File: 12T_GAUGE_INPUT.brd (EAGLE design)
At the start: 69.1 x 60 mm, 99 parts, among them J1 MICRO-SD_CARD_SOCKET, P1_WP_PULLUP 10k, P2_WP_PULLUP 10k, P3_WP_PULLUP 10k

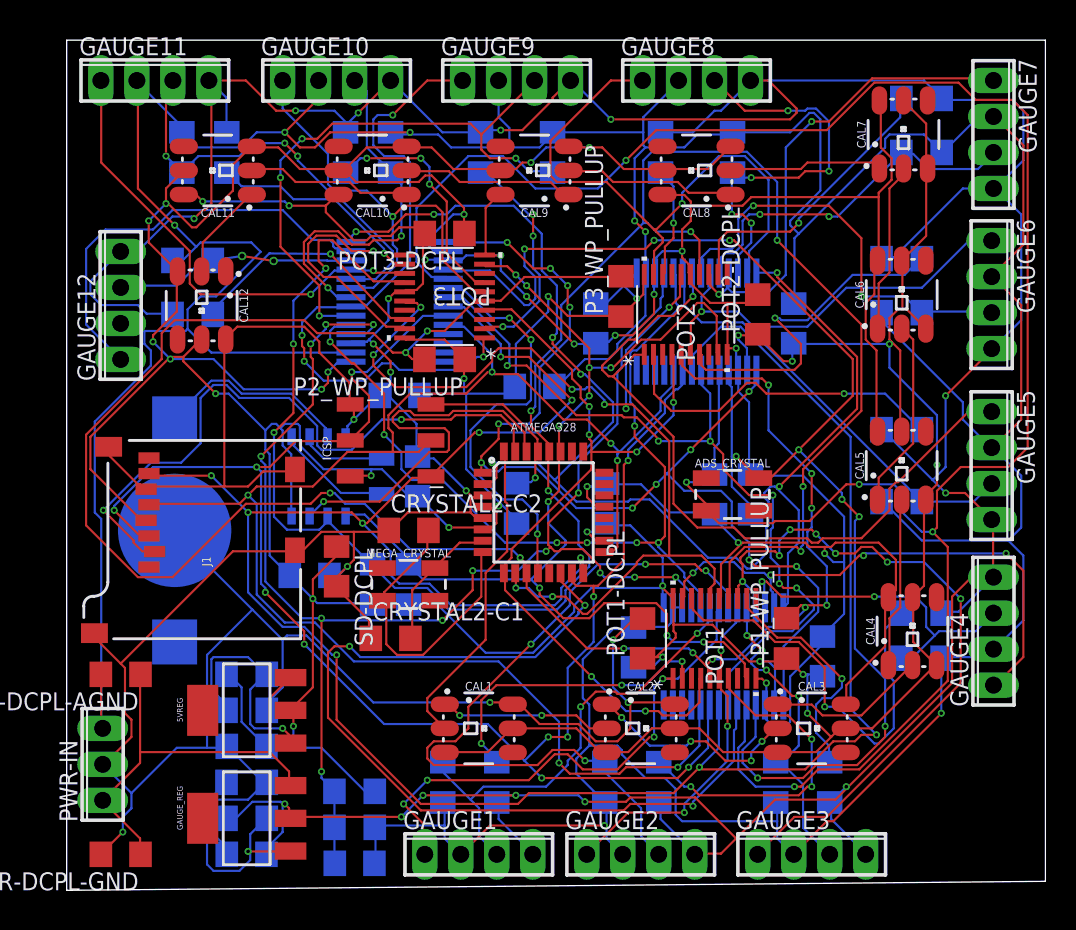
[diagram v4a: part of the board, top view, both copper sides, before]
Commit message: Converted to 4 layer board
Down to 2.3x2.7
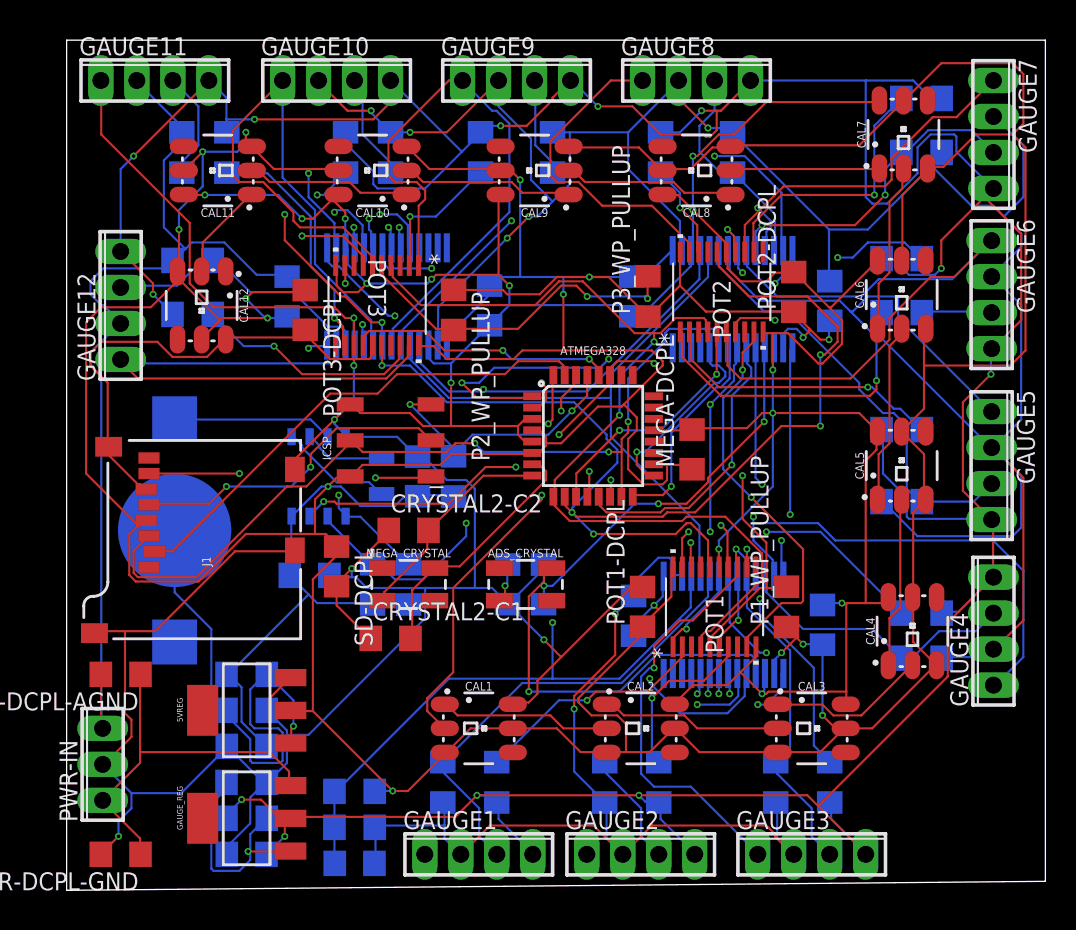
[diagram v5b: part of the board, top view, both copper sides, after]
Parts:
- moved ADS3-DCPL1 18.6 mm to (15.6, 41.9), turned to 90 degrees
- moved ADS_CRYSTAL 15.9 mm to (32.4, 21.6)
- moved CRYSTAL1-C1 15.9 mm to (31.1, 21.6)
- moved CRYSTAL1-C2 15.9 mm to (33.7, 21.6)
- moved POT3-DCPL 11.2 mm to (16.8, 41.0), turned to 270 degrees
- moved ADS3-DCPL2 8.98 mm to (29.8, 41.3), turned to 270 degrees
- moved MEGA-DCPL 7.13 mm to (44.1, 31.1), flipped to the top
- moved ATMEGA328 6.43 mm to (37.1, 32.1)
- moved MEGA_RESET_PULLUP 4.84 mm to (27.3, 29.2)
- moved POT3 4.80 mm to (21.9, 41.3), turned to 270 degrees
- moved P2_WP_PULLUP 3.55 mm to (27.3, 41.0), turned to 270 degrees
- moved ADS2-DCPL2 3.17 mm to (39.9, 41.9)
- moved ADS2 3.00 mm to (47.0, 41.7)
- moved ADS2-DCPL1 3.00 mm to (53.8, 41.6)
- moved POT2 3.00 mm to (46.2, 42.2)
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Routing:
- net MISO: track 173.3 -> 97.8 mm, vias 10 -> 5
- net WP: track 145.3 -> 73.2 mm, vias 12 -> 5
- net SCL: track 146.1 -> 81.8 mm, vias 9 -> 5
- net XTAL1: track 156.5 -> 95.2 mm, vias 5 -> 4
- net +5V: track 428.6 -> 488.4 mm, vias 28 -> 17
- net ADS1_CS: track 64.9 -> 24.3 mm, vias 3 -> 2
- net ADS_SYNC: track 99.0 -> 75.9 mm, vias 7 -> 4
- net ADS2_CS: track 0.00 -> 20.6 mm, vias 0 -> 1
- net B2+: track 52.3 -> 32.3 mm, vias 4 -> 1
- net MOSI: track 122.2 -> 102.4 mm, vias 11 -> 5
- net B6-_P2W1: track 29.8 -> 47.3 mm, vias 1 -> 0
- net B3-_P1W2: track 50.3 -> 32.8 mm, vias 7 -> 2
- net AINCOM: track 61.6 -> 44.8 mm, vias 7 -> 0
- net VREF: track 103.0 -> 87.6 mm, vias 13 -> 2
- net XTAL2: track 102.2 -> 87.3 mm, vias 9 -> 5
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
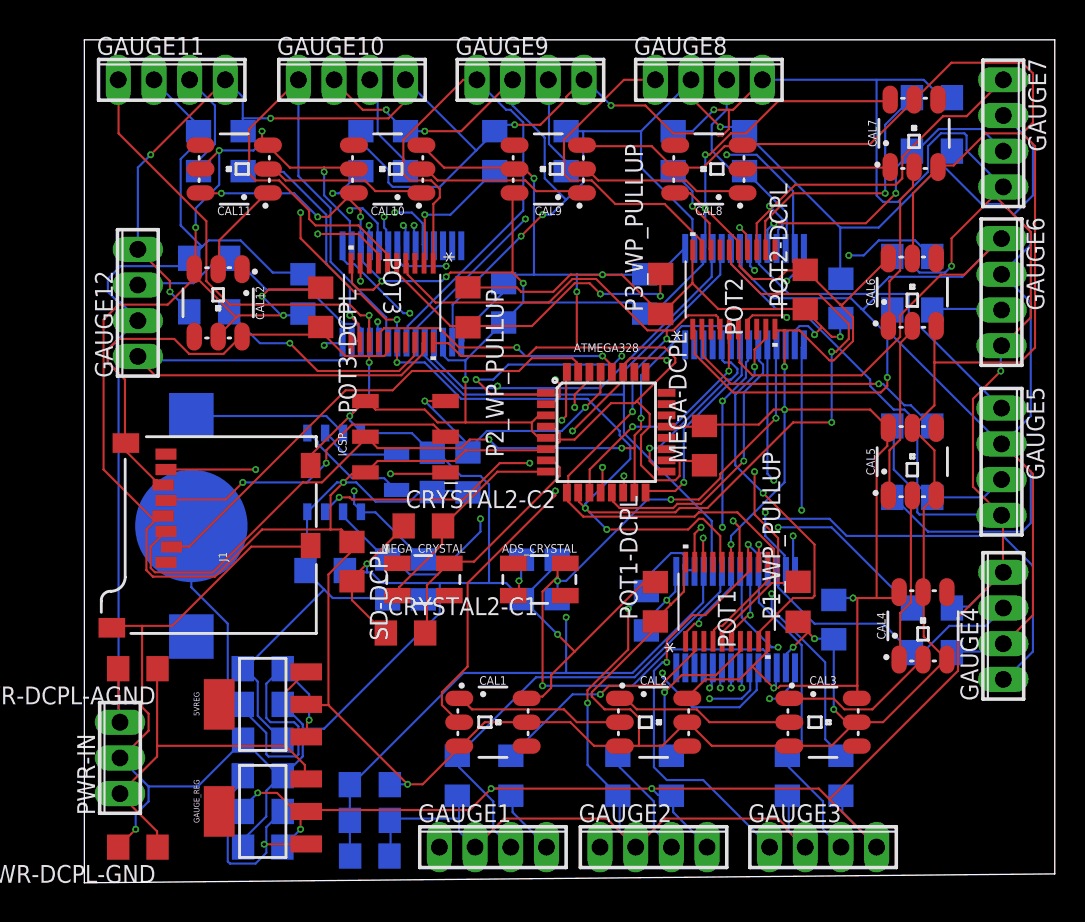
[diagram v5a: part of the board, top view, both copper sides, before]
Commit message: 4 Layer Size Optimization 2
Now 2.4x2.3
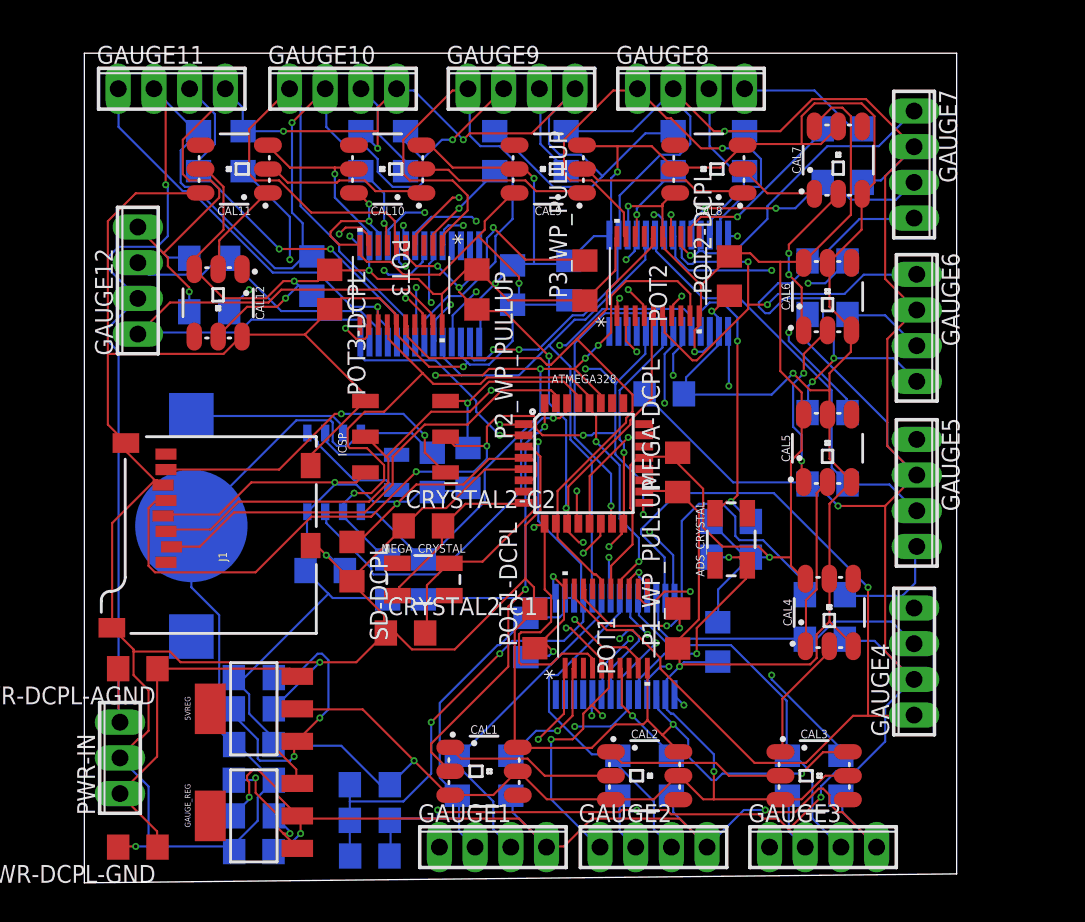
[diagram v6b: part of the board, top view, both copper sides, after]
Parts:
- moved CRYSTAL1-C1 15.0 mm to (46.0, 23.2), turned to 180 degrees
- moved ADS2-DCPL1 14.3 mm to (41.3, 34.8), turned to 0 degrees
- moved ADS_CRYSTAL 13.9 mm to (46.0, 24.4), turned to 90 degrees
- moved CRYSTAL1-C2 13.1 mm to (46.0, 25.7), turned to 0 degrees
- moved ADS1-DCPL1 8.78 mm to (31.4, 17.5)
- moved ADS1 8.78 mm to (37.8, 16.8)
- moved P1_WP_PULLUP 8.78 mm to (42.2, 18.1)
- moved POT1 8.78 mm to (37.1, 18.1)
- moved POT1-DCPL 8.78 mm to (32.1, 18.1)
- moved ADS1-DCPL2 8.41 mm to (45.1, 17.1)
- moved B4-R1 7.68 mm to (52.7, 17.3)
- moved B4-R2 7.68 mm to (52.7, 20.5)
- moved GAUGE4 6.84 mm to (59.1, 15.7)
- moved CAL4 6.74 mm to (53.0, 19.2)
- moved B7-R1 6.73 mm to (54.0, 49.8)
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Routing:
- net +5V: track 488.4 -> 398.2 mm, vias 17 -> 16
- net POT_SELECT_1: track 80.0 -> 47.3 mm, vias 5 -> 0
- net XTAL1: track 95.2 -> 65.0 mm
- net B4-_P1W3: track 42.0 -> 66.3 mm, vias 2 -> 1
- net GND: track 421.3 -> 442.5 mm, vias 19 -> 12
- net ADS_SYNC: track 75.9 -> 56.2 mm, vias 4 -> 3
- net VREF: track 87.6 -> 72.2 mm, vias 2 -> 5
- net B6-_P2W1: track 47.3 -> 32.4 mm, vias 0 -> 2
- net B5-_P2W0: track 48.9 -> 35.6 mm, vias 1 -> 2
- net XTAL2: track 87.3 -> 74.9 mm, vias 5 -> 4
- net AGND: track 355.3 -> 366.5 mm, vias 7 -> 10
- net MOSI: track 102.4 -> 91.6 mm, vias 5 -> 4
- net MISO: track 97.8 -> 87.2 mm, vias 5 -> 6
- net B1+: track 33.2 -> 23.6 mm
- net P1B3: track 19.3 -> 28.8 mm, vias 2 -> 1
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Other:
- board size 69.1 x 60 mm -> 62.1 x 59 mm

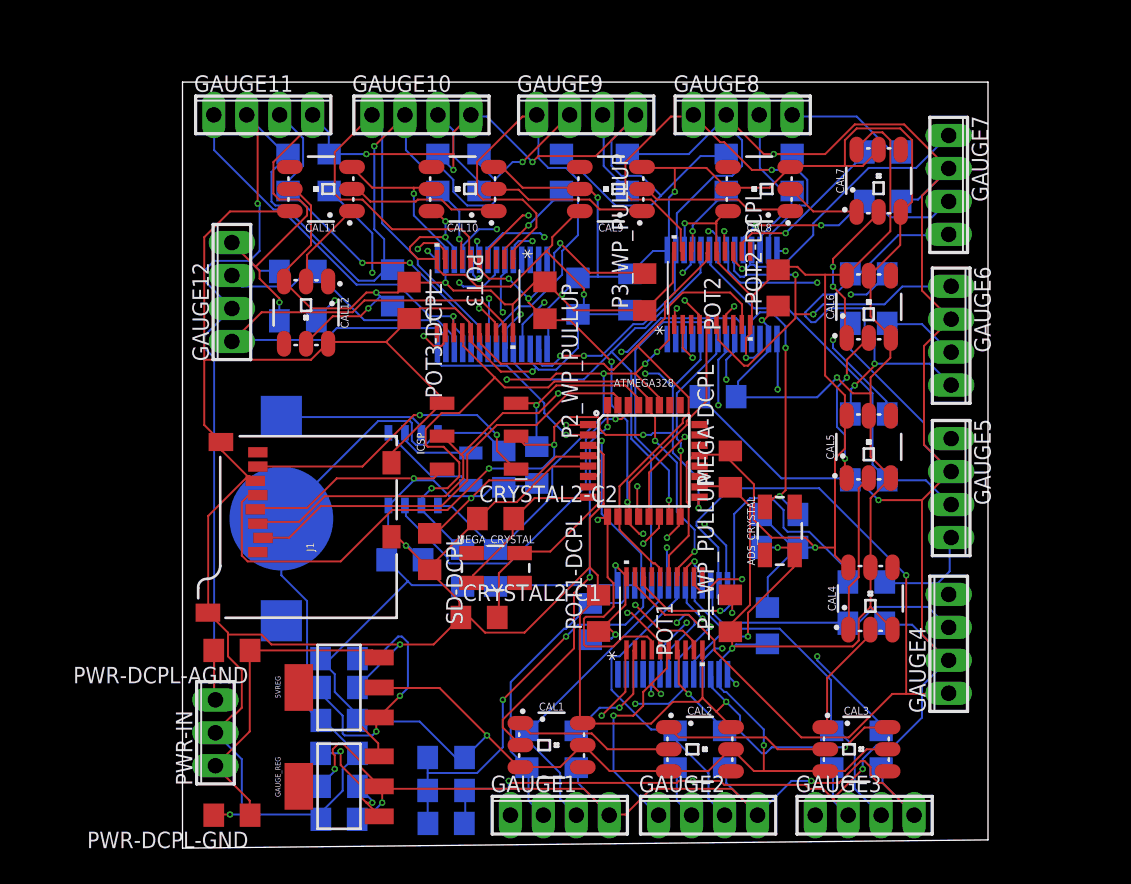
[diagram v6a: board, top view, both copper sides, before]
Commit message: Added in R3 to bridges
2.4x2.8"
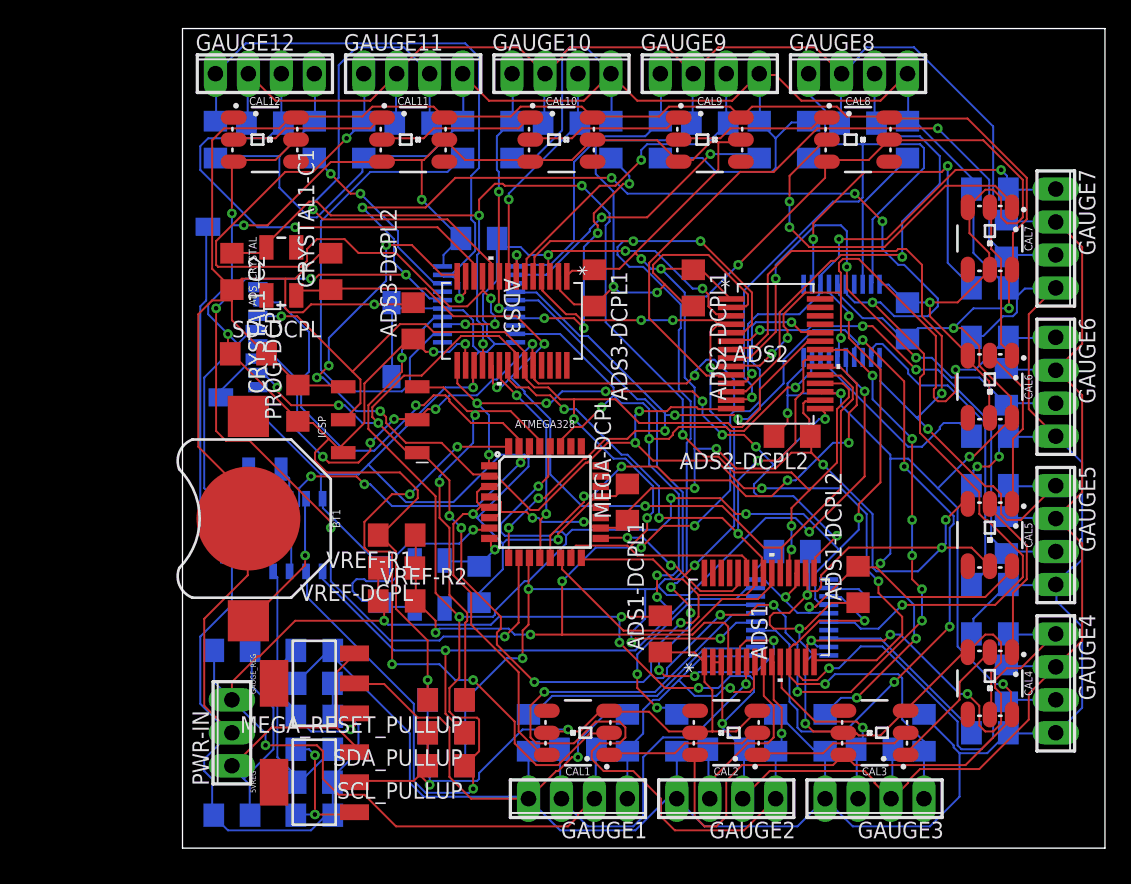
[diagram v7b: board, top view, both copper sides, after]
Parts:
- added B10R3, B11R3, B12R3, B1R3, B2R3, B3R3, B4R3, B5R3, B6R3, B7R3, B8R3, B9R3: 370, rcl:R1206
- moved CRYSTAL1-C2 46.2 mm to (3.81, 44.5), flipped to the top, turned to 270 degrees
- moved ADS_CRYSTAL 43.3 mm to (7.62, 44.5)
- moved CRYSTAL1-C1 40.6 mm to (11.4, 44.5), flipped to the top, turned to 90 degrees
- moved P3_WP_PULLUP 35.0 mm to (20.3, 11.4), flipped to the bottom, turned to 180 degrees
- moved P2_WP_PULLUP 34.2 mm to (20.3, 8.89), flipped to the bottom, turned to 180 degrees
- moved P1_WP_PULLUP 24.9 mm to (20.3, 6.35), flipped to the bottom, turned to 180 degrees
- moved SD-DCPL 20.7 mm to (5.08, 38.1), turned to 0 degrees
- moved VREF-DCPL 20.1 mm to (16.5, 21.6), flipped to the top
- moved MEGA_RESET_PULLUP 19.4 mm to (20.3, 11.4), flipped to the top, turned to 180 degrees
- moved VREF-R1 17.6 mm to (16.5, 24.1), flipped to the top
- moved GAUGE12 17.0 mm to (6.35, 59.7), turned to 0 degrees
- moved ADS2-DCPL2 16.7 mm to (47.0, 31.8), flipped to the top, turned to 180 degrees
- moved PROG-DCPL 16.7 mm to (8.89, 34.3), flipped to the top
- moved B5-R2 16.1 mm to (62.2, 20.3), turned to 0 degrees
- moved RTC_CRYSTAL 15.9 mm to (6.35, 29.2), turned to 0 degrees
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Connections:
- net N$2 renamed MEGA_XTAL1
- net N$21 renamed +3V
- net N$3 renamed MEGA_XTAL2
- net B1-_P1W0: now also B1R3.1
- net B10-_P3W1: now also B10R3.1
- net B11-_P3W2: now also B11R3.1
- net B12-_P3W3: now also B12R3.1
- net B2-_P1W1: now also B2R3.1
- net B3-_P1W2: now also B3R3.1
- net B4-_P1W3: now also B4R3.1
- net B5-_P2W0: now also B5R3.1
- net B6-_P2W1: now also B6R3.1
- net B7-_P2W2: now also B7R3.1
- net B8-_P2W3: now also B8R3.1
- net B9-_P3W0: now also B9R3.1
- net V+: now also B10R3.2, B11R3.2, B12R3.2, B1R3.2, B2R3.2, B3R3.2, B4R3.2, B5R3.2, B6R3.2, B7R3.2, B8R3.2, B9R3.2
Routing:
- net POT_SELECT_1: track 47.3 -> 176.7 mm, vias 0 -> 11
- net GND: track 442.5 -> 555.1 mm, vias 12 -> 16
- net +5V: track 398.2 -> 479.5 mm, vias 16 -> 23
- net SCL: track 74.5 -> 148.6 mm, vias 4 -> 8
- net V+: track 275.5 -> 332.1 mm, vias 9 -> 3
- net MISO: track 87.2 -> 143.3 mm, vias 6 -> 16
- net ADS_SYNC: track 56.2 -> 98.2 mm, vias 3 -> 8
- net AINCOM: track 40.5 -> 79.1 mm, vias 0 -> 7
- net B2-_P1W1: track 28.2 -> 64.9 mm, vias 3 -> 2
- net B7+: track 18.9 -> 55.0 mm, vias 2 -> 1
- net POT_SELECT_0: track 72.4 -> 105.3 mm, vias 3 -> 9
- net B4-_P1W3: track 66.3 -> 35.8 mm, vias 1 -> 3
- net ADS_RESET: track 81.7 -> 55.5 mm, vias 4 -> 9
- net B8+: track 12.9 -> 38.5 mm, vias 0 -> 1
- net B5-_P2W0: track 35.6 -> 59.9 mm
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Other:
- board size 62.1 x 59 mm -> 71.1 x 63.2 mm

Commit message: Ground plane
Maybe this will be finished. Maybe it won't.
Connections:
- removed net AGND: ADS1-DCPL1.2, ADS1.2, ADS1.3, ADS2-DCPL1.2, ADS2.2, ADS3-DCPL1.2, ADS3.2, B1-R1.1, B10-R1.1, B11-R1.1, B12-R1.1, B2-R1.1, B3-R1.1, B4-R1.1, B5-R1.1, B6-R1.1, B7-R1.1, B8-R1.1, B9-R1.1, GAUGE1.2, GAUGE10.2, GAUGE11.2, GAUGE12.2, GAUGE2.2, GAUGE3.2, GAUGE4.2, GAUGE5.2, GAUGE6.2, GAUGE7.2, GAUGE8.2, GAUGE9.2, PWR-DCPL-AGND.2, PWR-IN.3, VREF-DCPL.2, VREF-R2.1
- net GND: now also ADS1-DCPL1.2, ADS1.2, ADS1.3, ADS2-DCPL1.2, ADS2.2, ADS3-DCPL1.2, ADS3.2, B1-R1.1, B10-R1.1, B11-R1.1, B12-R1.1, B2-R1.1, B3-R1.1, B4-R1.1, B5-R1.1, B6-R1.1, B7-R1.1, B8-R1.1, B9-R1.1, GAUGE1.2, GAUGE10.2, GAUGE11.2, GAUGE12.2, GAUGE2.2, GAUGE3.2, GAUGE4.2, GAUGE5.2, GAUGE6.2, GAUGE7.2, GAUGE8.2, GAUGE9.2, PWR-DCPL-AGND.2, PWR-IN.3, VREF-DCPL.2, VREF-R2.1
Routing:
- net AGND: track 346.7 -> 0.00 mm, vias 8 -> 0
- net GND: track 555.1 -> 398.1 mm, vias 16 -> 111
- net V+: track 332.1 -> 320.4 mm, vias 3 -> 4
- net +12V: track 34.3 -> 30.0 mm, vias 0 -> 1
- net XTAL2: track 95.5 -> 98.0 mm
- net SCL: track 148.6 -> 150.4 mm
- net AINCOM: track 79.1 -> 77.4 mm
- net POT_SELECT_1: track 176.7 -> 178.3 mm
- net WP: track 104.5 -> 105.7 mm
- net B8+: track 38.5 -> 37.5 mm
- net P3B3: track 14.6 -> 15.6 mm
- net B5-_P2W0: track 59.9 -> 60.9 mm
- net B4+: track 29.2 -> 28.2 mm
- net POT_SELECT_0: track 105.3 -> 106.0 mm
- net B8-_P2W3: track 54.0 -> 54.7 mm
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- added copper zone on layer 1, net GND
- added copper zone on layer 16, net GND
